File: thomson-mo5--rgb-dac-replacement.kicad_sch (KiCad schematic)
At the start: 2 parts, among them J101 Input, J102 Output

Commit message: Done schematis
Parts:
- added Q101, Q102, Q103: 2N3904, symbol Device:Q_PNP_EBC
- added R101, R105, R109: 1K5, symbol Device:R_Small_US
- added R102, R106, R110: 3K, symbol Device:R_Small_US
- added R103, R107, R111: 6K2, symbol Device:R_Small_US
- added R104, R108, R112: 12K, symbol Device:R_Small_US
- added R113, R117, R121: 1K, symbol Device:R_Small_US
- added R114, R118, R122: 2K, symbol Device:R_Small_US
- added R115, R119, R123: 75, symbol Device:R_Small_US
- added R116, R120, R124: 150, symbol Device:R_Small_US
- added U101: QUADRUPLE_2-INPUTS_POSITIVE-OR_GATES, Package_DIP:DIP-14_W7.62mm_LongPads, symbol 74x32:QUADRUPLE_2-INPUTS_POSITIVE-OR_GATES
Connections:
- net +5V: now also Q101.3 (C), Q102.3 (C), Q103.3 (C), R113.2, R117.2, R121.2, U101.14 (VCC)
- net B1: now also R110.1, U101.9 (3A)
- net B2: now also R109.1, U101.10 (3B)
- net GND: now also R114.1, R116.1, R118.1, R120.1, R122.1, R124.1, U101.12 (4A), U101.13 (4B), U101.7 (GND)
- net R1: now also R102.1, U101.1 (1A)
- net R2: now also R101.1, U101.2 (1B)
- net VID_BLUE: now also R123.2
- net VID_GREEN: now also R119.2
- net VID_RED: now also R115.2
- net V1 renamed G1
- net G1: now also R106.1, U101.4 (2A)
- net V2 renamed G2
- net G2: now also R105.1, U101.5 (2B)
- new net: Q101.1 (E), R115.1, R116.2
- new net: Q101.2 (B), R101.2, R102.2, R103.2, R104.2, R113.1, R114.2
- new net: Q102.1 (E), R119.1, R120.2
- new net: Q102.2 (B), R105.2, R106.2, R107.2, R108.2, R117.1, R118.2
- new net: Q103.1 (E), R123.1, R124.2
- new net: Q103.2 (B), R109.2, R110.2, R111.2, R112.2, R121.1, R122.2
- new net B0: R111.1, R112.1, U101.8 (3Y)
- new net G0: R107.1, R108.1, U101.6 (2Y)
- new net R0: R103.1, R104.1, U101.3 (1Y)
- no-connect marks 1 -> 2
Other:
- moved on the sheet: J101, J102

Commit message: Done PCB
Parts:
- J1: renamed from J101; footprint (none) -> Connector_PinHeader_2.54mm:PinHeader_1x09_P2.54mm_Vertical
- J2: renamed from J102; footprint (none) -> Connector_PinHeader_2.54mm:PinHeader_1x03_P2.54mm_Vertical
- Q1: renamed from Q101; footprint (none) -> Package_TO_SOT_THT:TO-92_Inline_Wide
- Q2: renamed from Q102; footprint (none) -> Package_TO_SOT_THT:TO-92_Inline_Wide
- Q3: renamed from Q103; footprint (none) -> Package_TO_SOT_THT:TO-92_Inline_Wide
- R1: renamed from R101; footprint (none) -> commons-passives_THT:Passive_THT_resistor_W2.54mm_L12.70mm
- R10: renamed from R110; footprint (none) -> commons-passives_THT:Passive_THT_resistor_W2.54mm_L12.70mm
- R11: renamed from R111; footprint (none) -> commons-passives_THT:Passive_THT_resistor_W2.54mm_L12.70mm
- R12: renamed from R112; footprint (none) -> commons-passives_THT:Passive_THT_resistor_W2.54mm_L12.70mm
- R13: renamed from R113; footprint (none) -> commons-passives_THT:Passive_THT_resistor_W2.54mm_L12.70mm
- R14: renamed from R117; footprint (none) -> commons-passives_THT:Passive_THT_resistor_W2.54mm_L12.70mm
- R15: renamed from R121; footprint (none) -> commons-passives_THT:Passive_THT_resistor_W2.54mm_L12.70mm
- R16: renamed from R114; footprint (none) -> commons-passives_THT:Passive_THT_resistor_W2.54mm_L12.70mm
- R17: renamed from R118; footprint (none) -> commons-passives_THT:Passive_THT_resistor_W2.54mm_L12.70mm
- R18: renamed from R122; footprint (none) -> commons-passives_THT:Passive_THT_resistor_W2.54mm_L12.70mm
- R19: renamed from R116; footprint (none) -> commons-passives_THT:Passive_THT_resistor_W2.54mm_L12.70mm
- R2: renamed from R102; footprint (none) -> commons-passives_THT:Passive_THT_resistor_W2.54mm_L12.70mm
- R20: renamed from R120; footprint (none) -> commons-passives_THT:Passive_THT_resistor_W2.54mm_L12.70mm
- R21: renamed from R124; footprint (none) -> commons-passives_THT:Passive_THT_resistor_W2.54mm_L12.70mm
- R22: renamed from R115; footprint (none) -> commons-passives_THT:Passive_THT_resistor_W2.54mm_L12.70mm
- R23: renamed from R119; footprint (none) -> commons-passives_THT:Passive_THT_resistor_W2.54mm_L12.70mm
- R24: renamed from R123; footprint (none) -> commons-passives_THT:Passive_THT_resistor_W2.54mm_L12.70mm
- R3: renamed from R103; footprint (none) -> commons-passives_THT:Passive_THT_resistor_W2.54mm_L12.70mm
- R4: renamed from R104; footprint (none) -> commons-passives_THT:Passive_THT_resistor_W2.54mm_L12.70mm
- R5: renamed from R105; footprint (none) -> commons-passives_THT:Passive_THT_resistor_W2.54mm_L12.70mm
- R6: renamed from R106; footprint (none) -> commons-passives_THT:Passive_THT_resistor_W2.54mm_L12.70mm
- R7: renamed from R107; footprint (none) -> commons-passives_THT:Passive_THT_resistor_W2.54mm_L12.70mm
- R8: renamed from R108; footprint (none) -> commons-passives_THT:Passive_THT_resistor_W2.54mm_L12.70mm
- R9: renamed from R109; footprint (none) -> commons-passives_THT:Passive_THT_resistor_W2.54mm_L12.70mm
- renumbered U101 to U1

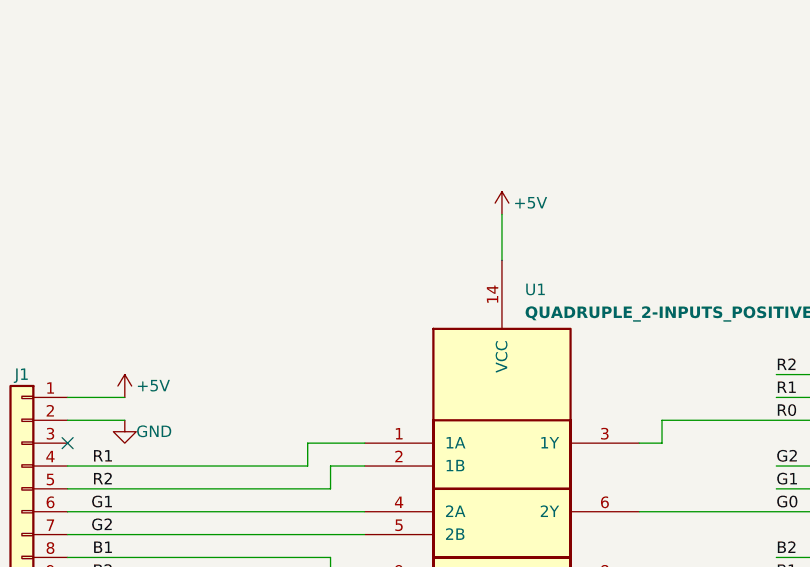
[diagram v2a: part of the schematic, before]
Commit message: Added decoupling capacitor
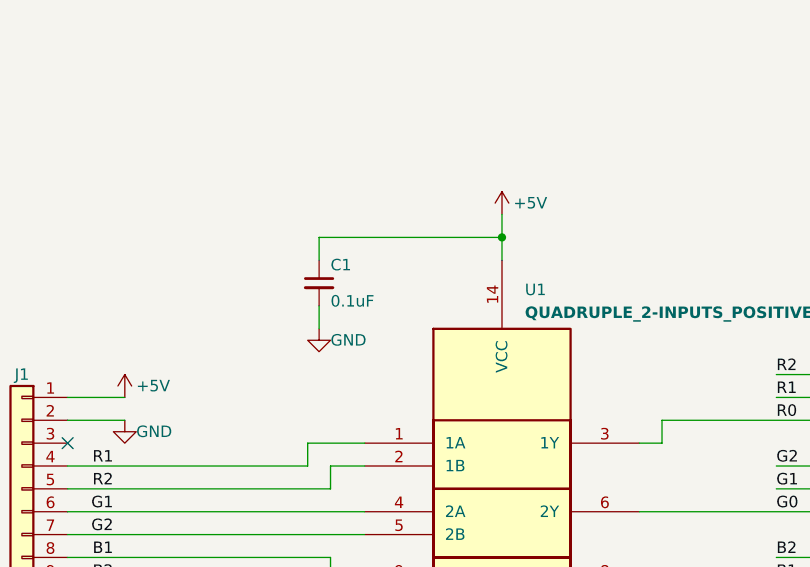
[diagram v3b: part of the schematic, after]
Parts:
- added C1: 0.1uF, commons-passives_THT:Passive_THT_capacitor_mlcc_W2.54mm_L5.08mm, symbol Device:C_Small
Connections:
- net +5V: now also C1.1
- net GND: now also C1.2
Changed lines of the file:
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@@
   (junction (at 128.27 101.6) (diameter 0) (color 0 0 0 0)
+  )
+  (junction (at 78.74 73.66) (diameter 0) (color 0 0 0 0)
   )
   (junction (at 128.27 104.14) (diameter 0) (color 0 0 0 0)
@@
     (stroke (width 0) (type default))
   )
+  (wire (pts (xy 58.42 81.28) (xy 58.42 83.82))
+    (stroke (width 0) (type default))
+  )
   (wire (pts (xy 114.3 93.98) (xy 96.52 93.98))
     (stroke (width 0) (type default))
@@
     (stroke (width 0) (type default))
   )
+  (wire (pts (xy 78.74 73.66) (xy 78.74 76.2))
+    (stroke (width 0) (type default))
+  )
   (wire (pts (xy 119.38 116.84) (xy 114.3 116.84))
     (stroke (width 0) (type default))
   )
+  (wire (pts (xy 58.42 76.2) (xy 58.42 73.66))
+    (stroke (width 0) (type default))
+  )
   (wire (pts (xy 119.38 106.68) (xy 114.3 106.68))
     (stroke (width 0) (type default))
@@
     (stroke (width 0) (type default))
   )
+  (wire (pts (xy 58.42 73.66) (xy 78.74 73.66))
+    (stroke (width 0) (type default))
+  )
   (wire (pts (xy 63.5 96.52) (xy 57.15 96.52))
     (stroke (width 0) (type default))
@@
     (stroke (width 0) (type default))
   )
-  (wire (pts (xy 78.74 71.12) (xy 78.74 76.2))
+  (wire (pts (xy 78.74 71.12) (xy 78.74 73.66))
     (stroke (width 0) (type default))
   )
@@
         (path "/6729e3ee-9a1a-4141-acef-0c5582111607"
           (reference "R14") (unit 1)
+        )
+      )
+    )
+  )
+  (symbol (lib_id "Device:C_Small") (at 58.42 78.74 0) (unit 1)
+    (in_bom yes) (on_board yes) (dnp no)
+    (property "Reference" "C1" (at 59.69 77.47 0)
+      (effects (font (size 1.27 1.27)) (justify left bottom))
+    )
+    (property "Value" "0.1uF" (at 59.69 80.01 0)
+      (effects (font (size 1.27 1.27)) (justify left top))
+    )
+    (property "Footprint" "commons-passives_THT:Passive_THT_capacitor_mlcc_W2.54mm_L5.08mm" (at 58.42 78.74 0)
+      (effects (font (size 1.27 1.27)) hide)
+    )
+    (property "Datasheet" "~" (at 58.42 78.74 0)
+      (effects (font (size 1.27 1.27)) hide)
+    )
+    (pin "2")
+    (pin "1")
+    (instances
+      (project "thomson-mo5--rgb-dac-replacement"
+        (path "/6729e3ee-9a1a-4141-acef-0c5582111607"
+          (reference "C1") (unit 1)
         )
       )
@@
         )
       )
+    )
+  )
+  (symbol (lib_id "power:GND") (at 58.42 83.82 0) (unit 1)
+    (in_bom yes) (on_board yes) (dnp no)
+    (property "Reference" "#PWR014" (at 58.42 90.17 0)
+      (effects (font (size 1.27 1.27)) hide)
+    )
+    (property "Value" "GND" (at 59.69 85.09 0)
+      (effects (font (size 1.27 1.27)) (justify left))
+    )
+    (property "Footprint" "" (at 58.42 83.82 0)
+      (effects (font (size 1.27 1.27)) hide)
+    )
+    (property "Datasheet" "" (at 58.42 83.82 0)
+      (effects (font (size 1.27 1.27)) hide)
+    )
+    (pin "1")
+    (instances
+      (project "thomson-mo5--rgb-dac-replacement"
+        (path "/6729e3ee-9a1a-4141-acef-0c5582111607"
+          (reference "#PWR014") (unit 1)
+        )
+      )

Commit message: Final tunings in layout (schematic and pcb)
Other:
- moved on the sheet: R1, R10, R11, R12, R2, R3, R4, R9

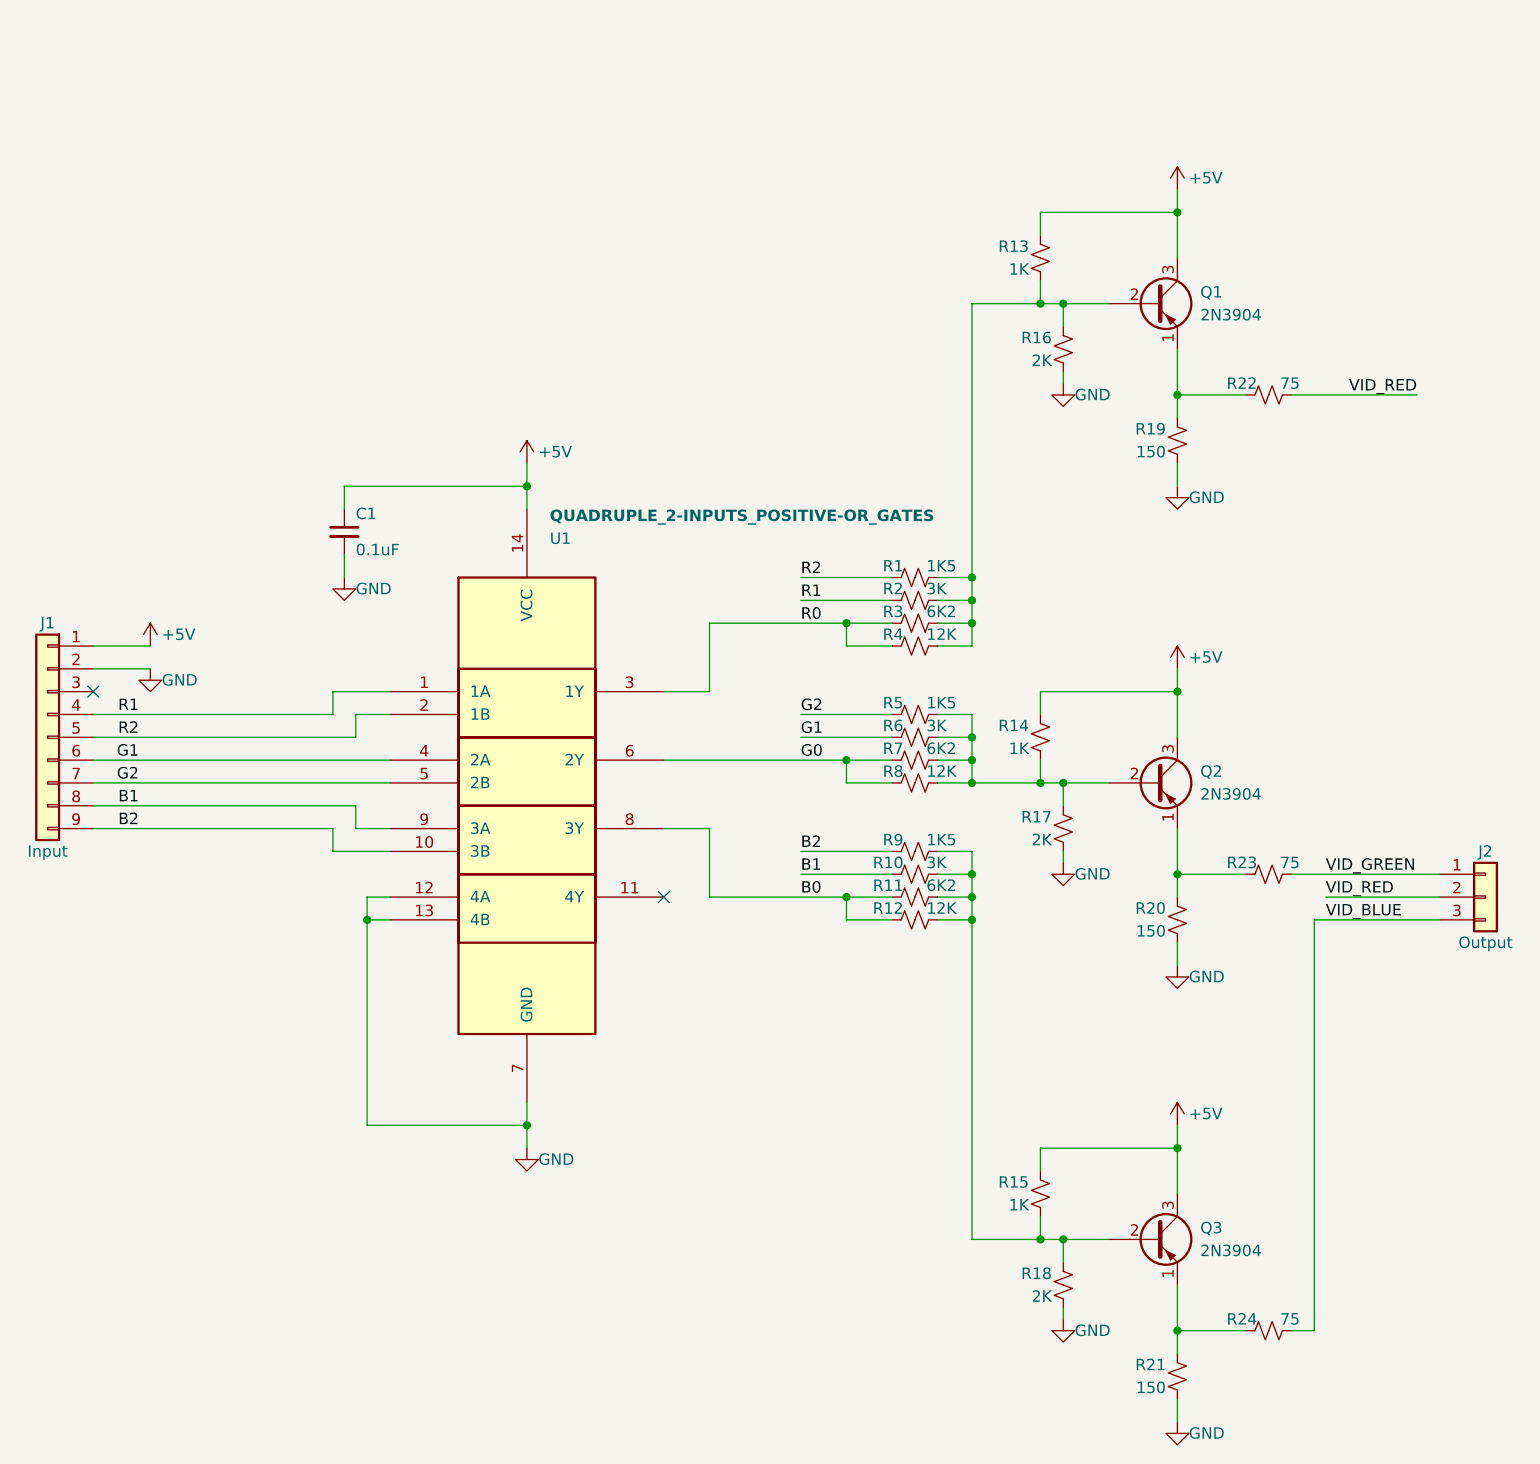
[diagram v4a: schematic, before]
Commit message: Resolves #1 : [schematic] Simplify the conversion
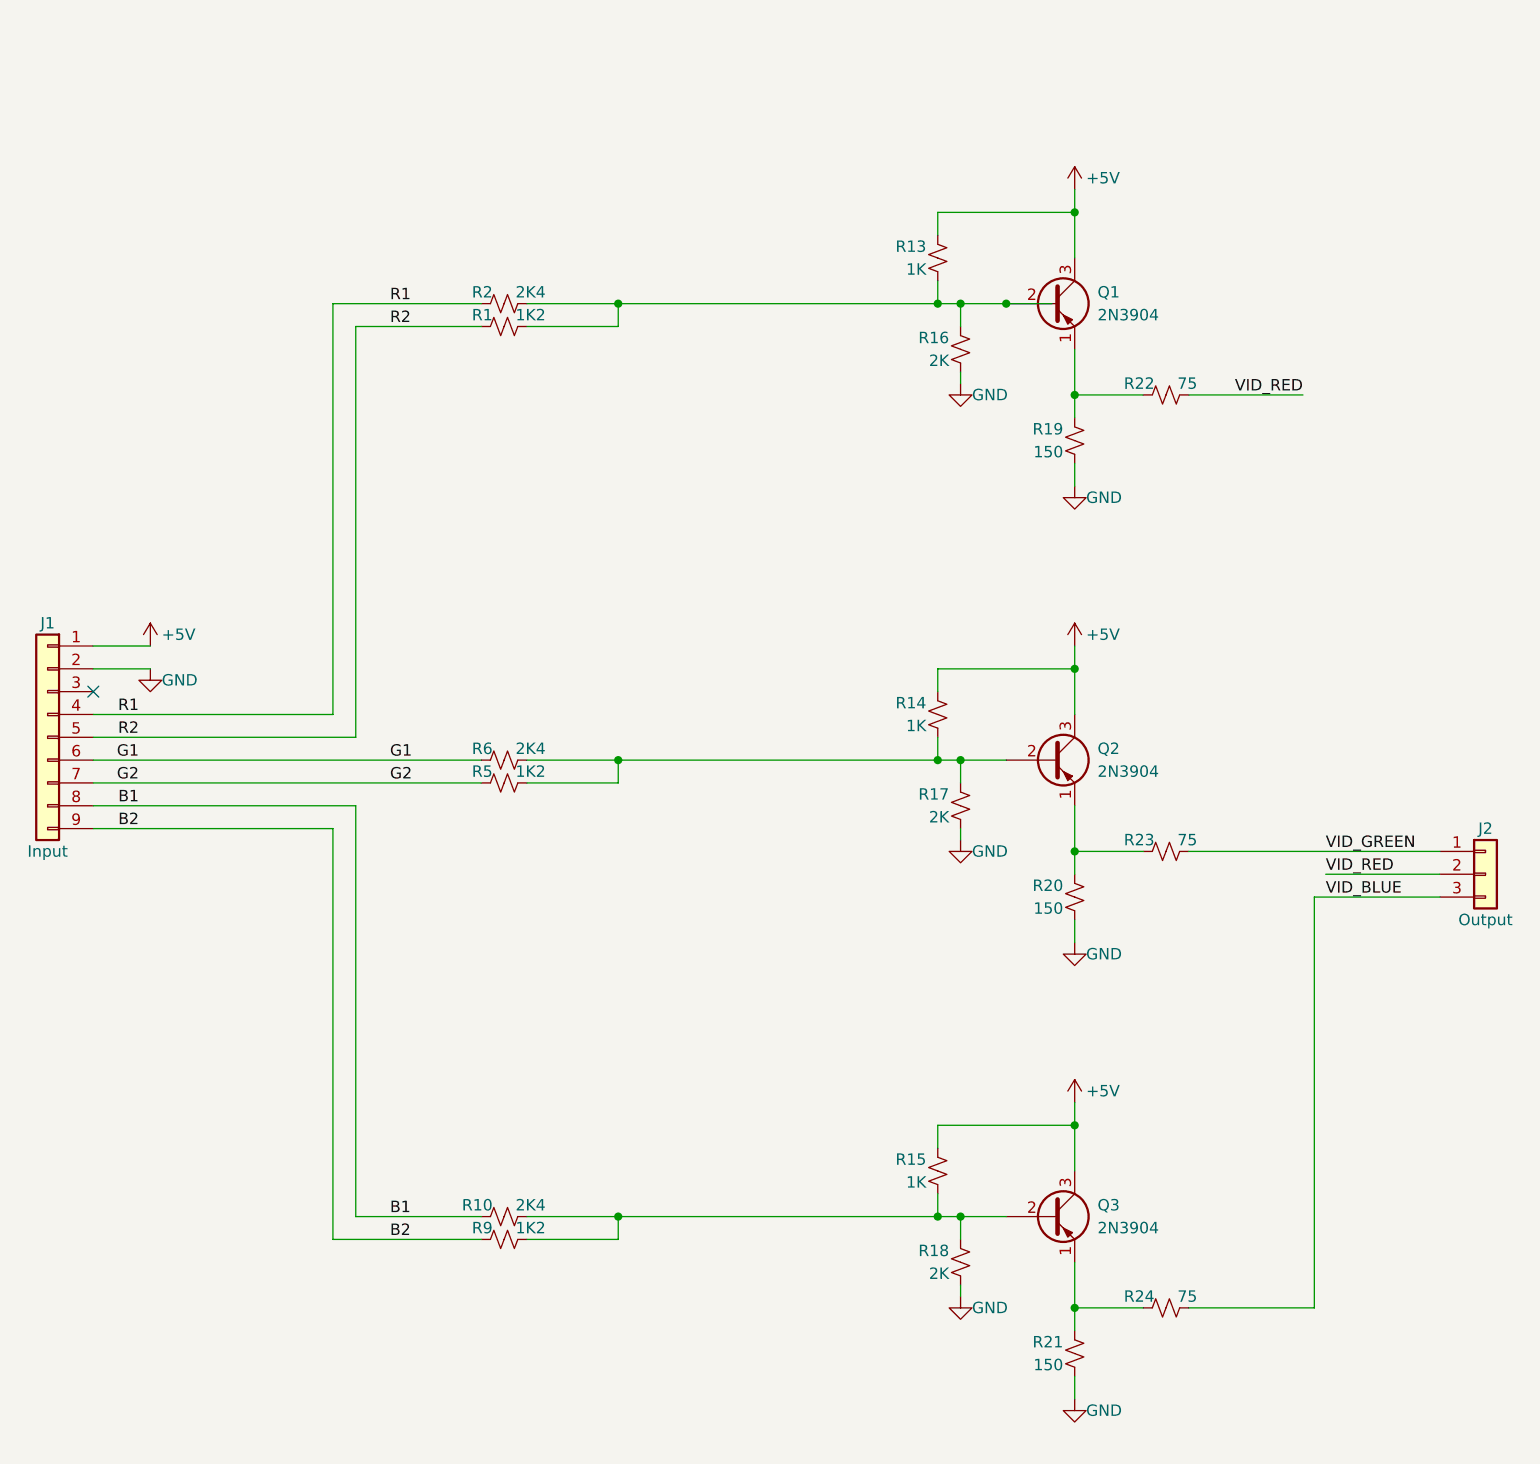
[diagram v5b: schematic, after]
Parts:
- removed C1: 0.1uF, commons-passives_THT:Passive_THT_capacitor_mlcc_W2.54mm_L5.08mm, symbol Device:C_Small
- removed R11, R3, R7: 6K2, commons-passives_THT:Passive_THT_resistor_W2.54mm_L12.70mm, symbol Device:R_Small_US
- removed R12, R4, R8: 12K, commons-passives_THT:Passive_THT_resistor_W2.54mm_L12.70mm, symbol Device:R_Small_US
- removed U1: QUADRUPLE_2-INPUTS_POSITIVE-OR_GATES, Package_DIP:DIP-14_W7.62mm_LongPads, symbol 74x32:QUADRUPLE_2-INPUTS_POSITIVE-OR_GATES
- R1, R5, R9: value 1K5 -> 1K2
- R10, R2, R6: value 3K -> 2K4
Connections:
- no-connect marks 2 -> 1
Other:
- moved on the sheet: J2, Q1, Q2, Q3, R1, R10, R13, R14, R15, R16, R17, R18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
